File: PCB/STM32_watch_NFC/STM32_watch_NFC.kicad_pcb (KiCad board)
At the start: 4 copper layers, 70 x 100 mm, 287 parts, among them J1 Conn_01x06_Socket, J2 USB_C_Receptacle_PowerOnly_6P, Q1 2N7000, SW1 SW_DPST_x2, SW2 SW_DPST_x2, SW3 SW_DPST_x2, U1 STM32L031G6Ux, U2 MIC5365-3.3YC5, U3 ST25R3916-AQWT, U4 MT3608, Y1 27.12Mhz, Y2 32.768kHz

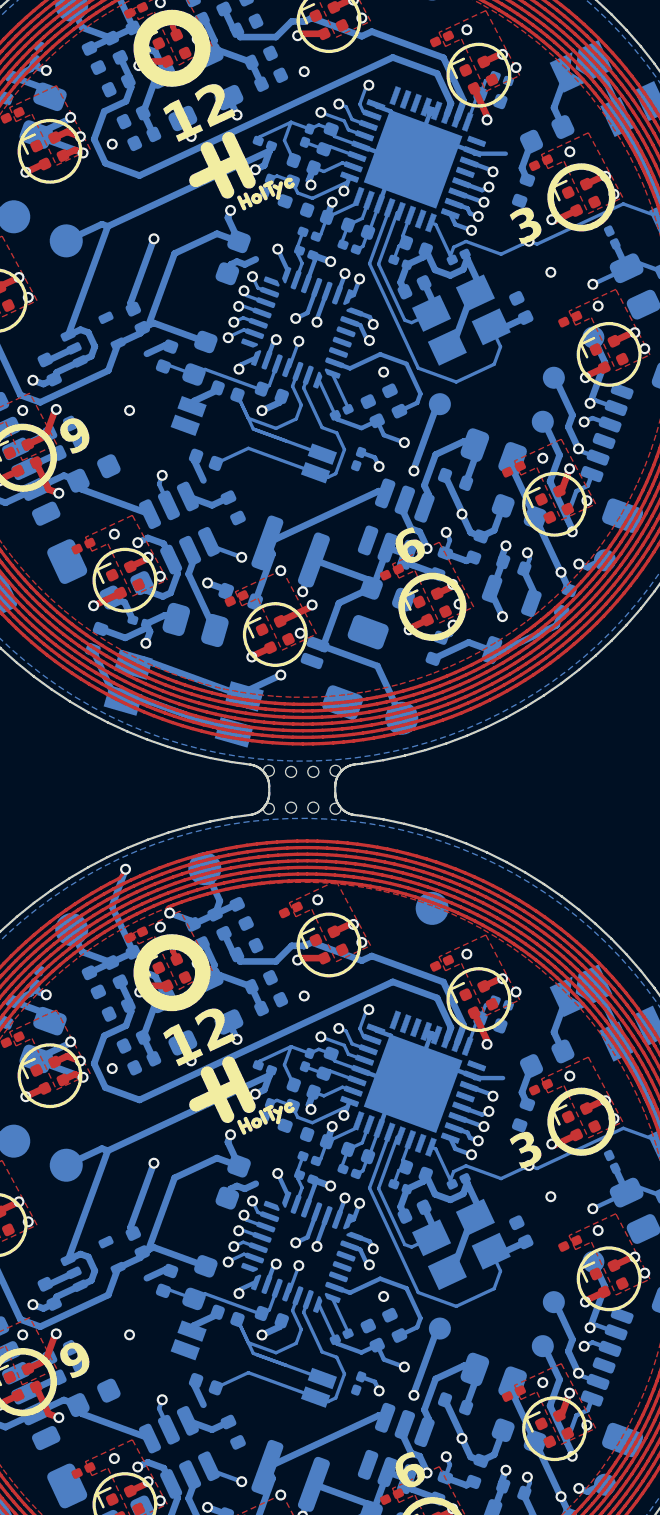
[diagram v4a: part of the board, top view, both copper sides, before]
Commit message: CODING #5 working Time and ADC for battery value
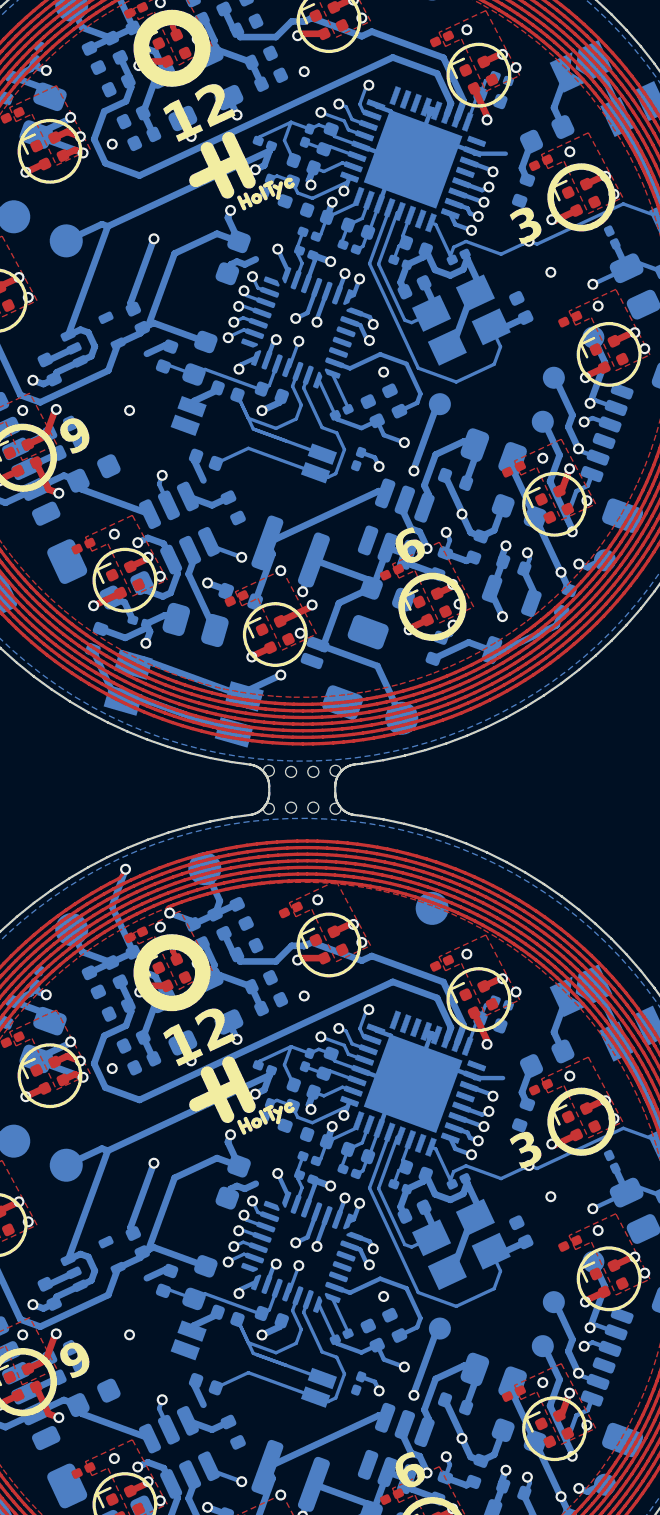
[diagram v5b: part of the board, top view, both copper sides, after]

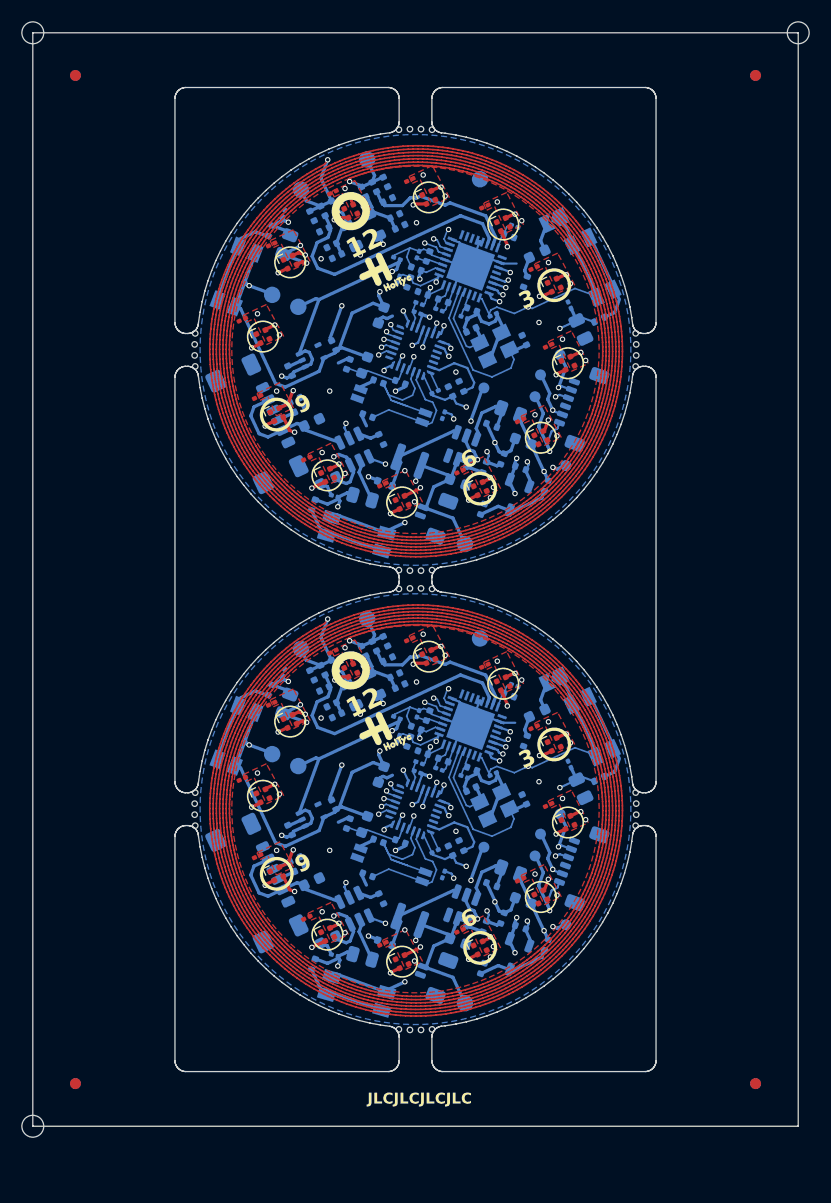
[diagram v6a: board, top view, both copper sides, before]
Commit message: URX watch #1
pcb is NOT panelizated
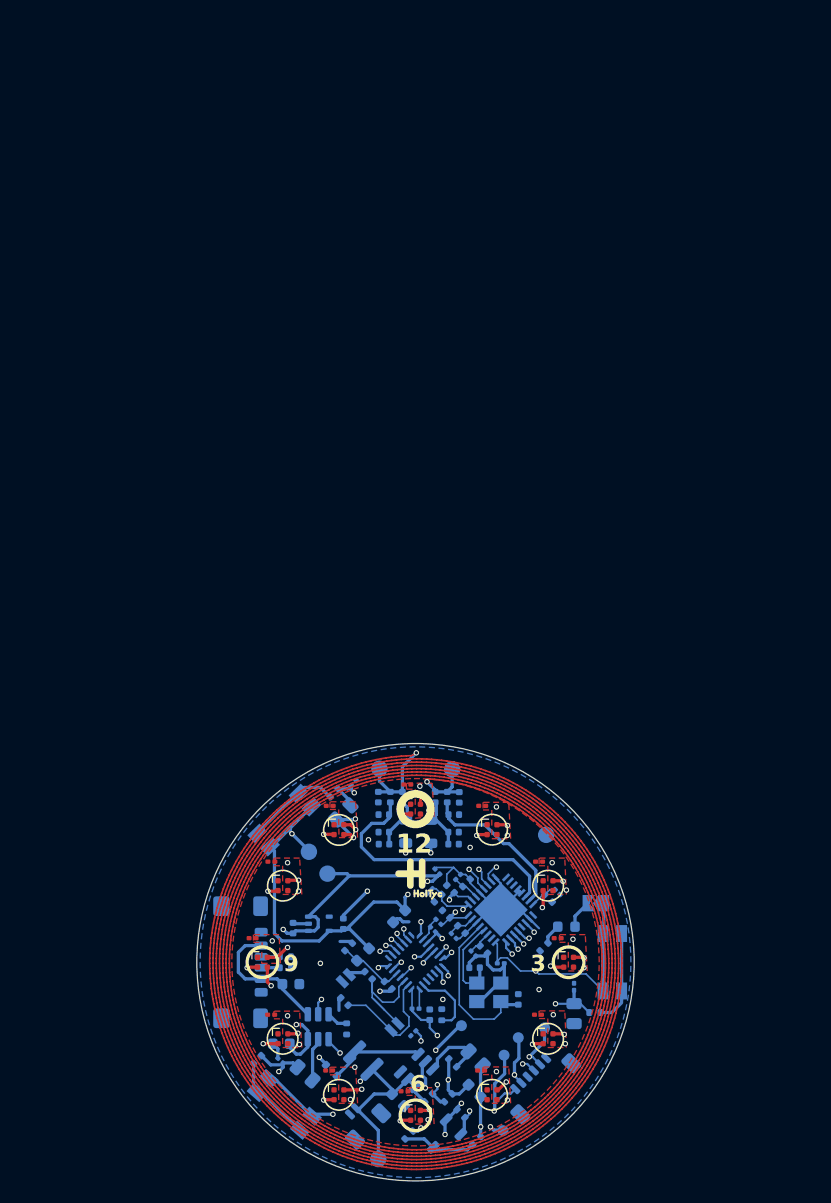
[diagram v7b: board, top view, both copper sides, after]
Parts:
- removed the +BAT at (153.0, 108.8)
- removed the +BAT at (153.0, 66.8)
- removed the 3V3 at (135.4, 44.0)
- removed the 3V3 at (135.4, 86.0)
- removed the 5V at (137.8, 87.1)
- removed the 5V at (137.8, 45.1)
- removed the A1 at (138.0, 34.4)
- removed the A1 at (138.0, 76.4)
- removed the A2 at (144.1, 31.6)
- removed the A2 at (144.1, 73.6)
- removed the CLK at (159.4, 53.3)
- removed the CLK at (159.4, 95.3)
- removed the DINS at (162.3, 59.6)
- removed the DINS at (162.3, 101.6)
- removed the DIO at (159.9, 93.3)
- removed the DIO at (159.9, 51.3)
- removed the D_BAT at (154.8, 52.5)
- removed the D_BAT at (154.8, 94.5)
- removed the G*** at (145.8, 41.9)
- removed the G*** at (145.8, 83.9)
- removed the GND at (154.4, 33.4)
- removed the GND at (154.4, 75.4)
- removed the JP1 at (161.2, 37.1)
- removed the JP1 at (161.2, 79.1)
- removed KiKit_FID_B_1, KiKit_FID_B_2, KiKit_FID_B_3, KiKit_FID_B_4, KiKit_FID_T_1, KiKit_FID_T_2, KiKit_FID_T_3, KiKit_FID_T_4: Fiducial, Fiducial
- removed KiKit_MB_1_1, KiKit_MB_1_2, KiKit_MB_1_3, KiKit_MB_1_4, KiKit_MB_2_1, KiKit_MB_2_2, KiKit_MB_2_3, KiKit_MB_2_4, KiKit_MB_3_1, KiKit_MB_3_2, KiKit_MB_3_3, KiKit_MB_3_4, KiKit_MB_4_1, KiKit_MB_4_2, KiKit_MB_4_3, KiKit_MB_4_4, KiKit_MB_5_1, KiKit_MB_5_2, KiKit_MB_5_3, KiKit_MB_5_4, KiKit_MB_6_1, KiKit_MB_6_2, KiKit_MB_6_3, KiKit_MB_6_4, KiKit_MB_7_1, KiKit_MB_7_2, KiKit_MB_7_3, KiKit_MB_7_4, KiKit_MB_8_1, KiKit_MB_8_2, KiKit_MB_8_3, KiKit_MB_8_4, KiKit_TO_1, KiKit_TO_2, KiKit_TO_3: NPTH, NPTH
- removed the NRST at (161.7, 91.5)
- removed the NRST at (161.7, 49.5)
- removed TC1, TC12, TC13, TC14, TC15, TC16, TC17, TC18, TC19, TC2, TC20, TC21, TC22, TC23, TC28, TC29, TC30, TC31, TC7: 100n, Capacitor_SMD:C_0201_0603Metric
- removed TC10, TC11, TC46, TC5, TC6: 1u, Capacitor_SMD:C_0402_1005Metric
- removed TC24, TC25, TC26, TC27, TC4: 10u, Capacitor_SMD:C_0603_1608Metric
- removed TC3: 10n, Capacitor_SMD:C_0402_1005Metric
- removed TC34, TC36, TC38, TC40, TC42, TC44, TC47: 22n, Capacitor_SMD:C_0201_0603Metric
- removed TC35, TC37, TC39, TC41, TC43, TC45: 2.2uF, Capacitor_SMD:C_0402_1005Metric
- removed TC48, TC49, TC50, TC51, TC58, TC59, TC8, TC9: 15pF, Capacitor_SMD:C_0402_1005Metric
- removed TC52, TC53, TC54, TC55, TC57, TC61: 220pF, Capacitor_SMD:C_0402_1005Metric
- removed TC56, TC60: 10pF, Capacitor_SMD:C_0402_1005Metric
- removed TD1, TD10, TD11, TD12, TD2, TD3, TD4, TD5, TD6, TD7, TD8, TD9: SK6805, LED_SMD:LED_SK6812_EC15_1.5x1.5mm
- removed TD13: D_Schottky, Diode_SMD:D_SOD-523
- removed TD14: LED, LED_SMD:LED_0603_1608Metric
- removed TFB1: FerriteBead, Inductor_SMD:L_0603_1608Metric
- removed TJ1: Conn_01x06_Socket, Connector_JST:JST_SUR_SM06B-SURS-TF_1x06-1MP_P0.80mm_Horizontal
- removed TJ2: USB_C_Receptacle_PowerOnly_6P, Connector_USB:USB_C_Receptacle_GCT_USB4135-GF-A_6P_TopMnt_Horizontal
- removed TL1: 22uH, Components:SLW3015
- removed TL2, TL3: 270nH 500mOhm, Inductor_SMD:L_0805_2012Metric
- removed TLi-po1: Conn_01x02_Socket, Connector_JST:JST_SUR_SM02B-SURS-TF_1x02-1MP_P0.80mm_Horizontal
- removed TME4055A1: ~, Package_TO_SOT_SMD:SOT-23-6
- removed TQ1: 2N7000, Package_TO_SOT_SMD:TSOT-23
- removed TR1, TR16, TR17, TR2, TR3: 10K, Resistor_SMD:R_0402_1005Metric
- removed TR10, TR12, TR14, TR8: 16.5K, Resistor_SMD:R_0805_2012Metric
- removed TR11, TR13, TR15, TR18, TR6: 510, Resistor_SMD:R_0402_1005Metric
- removed TR4, TR5, TR7: 5K1, Resistor_SMD:R_0402_1005Metric
- removed TR9: 2.2K, Resistor_SMD:R_0402_1005Metric
- removed TSW1, TSW2, TSW3: SW_DPST_x2, Button_Switch_SMD:Panasonic_EVQPUJ_EVQPUA
- removed TU1: STM32L031G6Ux, Package_DFN_QFN:QFN-28_4x4mm_P0.5mm
- removed TU2: MIC5365-3.3YC5, Package_TO_SOT_SMD:SOT-353_SC-70-5
- removed TU3: ST25R3916-AQWT, ST25R3916-AQWT:QFN50P500X500X100-33N
- removed TU4: MT3608, Package_TO_SOT_SMD:SOT-23-6
- removed TY1: 27.12Mhz, Crystal:Crystal_SMD_3225-4Pin_3.2x2.5mm
- removed TY2: 32.768kHz, Crystal:Crystal_SMD_SeikoEpson_MC146-4Pin_6.7x1.5mm
- added +BAT: 2.7-4.2V, TestPoint:TestPoint_Pad_D1.5mm, B.Cu at (145.1, 123.0)
- added 3V3: 3V3, TestPoint:TestPoint_Pad_D1.5mm, B.Cu at (138.8, 94.9)
- added 5V: 5V, TestPoint:TestPoint_Pad_D1.5mm, B.Cu at (140.4, 96.9)
- added A1: ~, TestPoint:TestPoint_Pad_D1.5mm, B.Cu at (145.2, 87.3)
- added A2: ~, TestPoint:TestPoint_Pad_D1.5mm, B.Cu at (151.8, 87.3)
- added CLK: ~, TestPoint:TestPoint_Pad_D1.0mm, B.Cu at (156.6, 113.5)
- added DINS: ~, TestPoint:TestPoint_Pad_D1.0mm, B.Cu at (156.5, 120.4)
- added DIO: ~, TestPoint:TestPoint_Pad_D1.0mm, B.Cu at (157.9, 111.9)
- added D_BAT: ~, TestPoint:TestPoint_Pad_D1.0mm, B.Cu at (152.7, 110.8)
- added G***: LOGO, LOGO, F.Cu at (149.1, 97.5)
- added GND: GND, TestPoint:TestPoint_Pad_D1.5mm, B.Cu at (160.4, 93.3)
- added JP1: SolderJumper_2_Open, Jumper:SolderJumper-2_P1.3mm_Open_TrianglePad1.0x1.5mm, B.Cu at (165.0, 99.6)
- added NRST: ~, TestPoint:TestPoint_Pad_D1.0mm, B.Cu at (160.3, 111.0)
- moved SW2 21.6 mm to (166.5, 105.0), turned to 90 degrees
- moved R15 21.4 mm to (164.9, 109.6), turned to 180 degrees
- moved R14 20.6 mm to (163.0, 109.7), turned to -90 degrees
- moved C30 20.3 mm to (163.0, 107.2), turned to -90 degrees
- moved J1 20.1 mm to (159.8, 116.0), turned to -135 degrees
- moved D4 20.0 mm to (162.5, 105.0), turned to 0 degrees
- moved D5 19.9 mm to (160.6, 112.0), turned to 0 degrees
- moved D14 19.7 mm to (162.3, 101.8), turned to 0 degrees
- moved C15 19.4 mm to (161.5, 102.8), turned to 0 degrees
- moved C47 19.3 mm to (161.5, 98.6), turned to -45 degrees
- moved C16 19.2 mm to (159.7, 109.8), turned to 0 degrees
- moved R2 19.0 mm to (154.1, 121.3), turned to -135 degrees
- moved C46 18.9 mm to (160.7, 99.2), turned to 135 degrees
- moved D3 18.9 mm to (160.6, 98.0), turned to 0 degrees
- moved R18 18.9 mm to (160.2, 103.6), turned to -135 degrees
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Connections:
- net Board_1-+3.3V renamed +3.3V
- net Board_1-+3.3VA renamed +3.3VA
- net Board_1-+5V renamed +5V
- net Board_1-+BATT renamed +BATT
- net Board_1-/LSE_IN renamed /LSE_IN
- net Board_1-/LSE_OUT renamed /LSE_OUT
- net Board_1-/NFC_RFID/A1 renamed /NFC_RFID/A1
- net Board_1-/NFC_RFID/A2 renamed /NFC_RFID/A2
- net Board_1-/NRST renamed /NRST
- net Board_1-/SWCLK renamed /SWCLK
- net Board_1-/SWDIO renamed /SWDIO
- net Board_1-BATT_STM renamed BATT_STM
- net Board_1-Button_LB renamed Button_LB
- net Board_1-Button_LT renamed Button_LT
- net Board_1-Button_R renamed Button_R
- net Board_1-CHRG_STM renamed CHRG_STM
- net Board_1-DIN_LED renamed DIN_LED
- net Board_1-DIN_STM renamed DIN_STM
- net Board_1-DONE_STM renamed DONE_STM
- net Board_1-GND renamed GND
- net Board_1-Net-(C50-Pad1) renamed Net-(C50-Pad1)
- net Board_1-Net-(C51-Pad1) renamed Net-(C51-Pad1)
- net Board_1-Net-(D1-DIN) renamed Net-(D1-DIN)
- net Board_1-Net-(D1-DOUT) renamed Net-(D1-DOUT)
- net Board_1-Net-(D10-DIN) renamed Net-(D10-DIN)
- net Board_1-Net-(D10-DOUT) renamed Net-(D10-DOUT)
- net Board_1-Net-(D11-DOUT) renamed Net-(D11-DOUT)
- net Board_1-Net-(D13-A) renamed Net-(D13-A)
- net Board_1-Net-(D14-K) renamed Net-(D14-K)
- net Board_1-Net-(D2-DOUT) renamed Net-(D2-DOUT)
- net Board_1-Net-(D3-DOUT) renamed Net-(D3-DOUT)
- net Board_1-Net-(D4-DOUT) renamed Net-(D4-DOUT)
- net Board_1-Net-(D5-DOUT) renamed Net-(D5-DOUT)
- net Board_1-Net-(D7-DIN) renamed Net-(D7-DIN)
- net Board_1-Net-(D7-DOUT) renamed Net-(D7-DOUT)
- net Board_1-Net-(D8-DOUT) renamed Net-(D8-DOUT)
- net Board_1-Net-(J2-CC1) renamed Net-(J2-CC1)
- net Board_1-Net-(J2-CC2) renamed Net-(J2-CC2)
- net Board_1-Net-(ME4055A1-PROG) renamed Net-(ME4055A1-PROG)
- net Board_1-Net-(SW1A-A) renamed Net-(SW1A-A)
- net Board_1-Net-(SW2A-A) renamed Net-(SW2A-A)
- net Board_1-Net-(SW3A-A) renamed Net-(SW3A-A)
- net Board_1-Net-(U1-BOOT0) renamed Net-(U1-BOOT0)
- net Board_1-Net-(U3-AGDC) renamed Net-(U3-AGDC)
- net Board_1-Net-(U3-RFI1) renamed Net-(U3-RFI1)
- net Board_1-Net-(U3-RFI2) renamed Net-(U3-RFI2)
- net Board_1-Net-(U3-RFO1) renamed Net-(U3-RFO1)
- net Board_1-Net-(U3-RFO2) renamed Net-(U3-RFO2)
- net Board_1-Net-(U3-VDD_A) renamed Net-(U3-VDD_A)
- net Board_1-Net-(U3-VDD_AM) renamed Net-(U3-VDD_AM)
- net Board_1-Net-(U3-VDD_D) renamed Net-(U3-VDD_D)
- net Board_1-Net-(U3-VDD_DR) renamed Net-(U3-VDD_DR)
- net Board_1-Net-(U3-XTI) renamed Net-(U3-XTI)
- net Board_1-Net-(U3-XTO) renamed Net-(U3-XTO)
- net Board_1-Net-(U4-FB) renamed Net-(U4-FB)
- net Board_1-SPI_CS_STM renamed SPI_CS_STM
- net Board_1-SPI_IRQ_STM renamed SPI_IRQ_STM
- net Board_1-SPI_MISO_STM renamed SPI_MISO_STM
- net Board_1-SPI_MOSI_STM renamed SPI_MOSI_STM
- net Board_1-SPI_SCL_STM renamed SPI_SCL_STM
- net Board_1-VBUS renamed VBUS
- D14 pad 2: Board_1-Net-(D14-A) -> Net-(D14-A)
- D6 pad 1: Board_1-unconnected-(D6-DOUT-Pad1) -> unconnected-(D6-DOUT-Pad1)
- J1 pad 1: Board_1-unconnected-(J1-Pin_1-Pad1) -> unconnected-(J1-Pin_1-Pad1)
- U1 pad 14: Board_1-unconnected-(U1-PB0-Pad14) -> unconnected-(U1-PB0-Pad14)
- U1 pad 24: Board_1-unconnected-(U1-PB3-Pad24) -> unconnected-(U1-PB3-Pad24)
- U1 pad 25: Board_1-unconnected-(U1-PB6-Pad25) -> unconnected-(U1-PB6-Pad25)
- U1 pad 26: Board_1-unconnected-(U1-PB7-Pad26) -> unconnected-(U1-PB7-Pad26)
- U1 pad 8: Board_1-unconnected-(U1-PA2-Pad8) -> unconnected-(U1-PA2-Pad8)
- U2 pad 4: Board_1-unconnected-(U2-NC-Pad4) -> unconnected-(U2-NC-Pad4)
- U3 pad 17: Board_1-unconnected-(U3-EXT_LM-Pad17) -> unconnected-(U3-EXT_LM-Pad17)
- U3 pad 18: Board_1-unconnected-(U3-AAT_A-Pad18) -> unconnected-(U3-AAT_A-Pad18)
- U3 pad 19: Board_1-unconnected-(U3-AAT_B-Pad19) -> unconnected-(U3-AAT_B-Pad19)
- U3 pad 2: Board_1-unconnected-(U3-CSO-Pad2) -> unconnected-(U3-CSO-Pad2)
- U3 pad 25: Board_1-unconnected-(U3-CSI-Pad25) -> unconnected-(U3-CSI-Pad25)
- U3 pad 28: Board_1-unconnected-(U3-MCU_CLK-Pad28) -> unconnected-(U3-MCU_CLK-Pad28)
- U4 pad 6: Board_1-unconnected-(U4-NC-Pad6) -> unconnected-(U4-NC-Pad6)
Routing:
- net Board_0-/NFC_RFID/A1: track 797.8 -> 0.00 mm, vias 1 -> 0
- net Board_0-GND: track 237.5 -> 0.00 mm, vias 32 -> 0
- net Board_0-+3.3V: track 152.2 -> 0.00 mm, vias 8 -> 0
- net Board_0-+5V: track 76.9 -> 0.00 mm, vias 6 -> 0
- net Board_0-/NRST: track 33.8 -> 0.00 mm, vias 3 -> 0
- net Board_0-+BATT: track 32.1 -> 0.00 mm, vias 2 -> 0
- net Board_0-/SWCLK: track 24.5 -> 0.00 mm, vias 2 -> 0
- net Board_0-Net-(U3-RFI1): track 24.3 -> 0.00 mm
- net Board_0-Button_LT: track 24.3 -> 0.00 mm, vias 2 -> 0
- net Board_0-DIN_STM: track 23.0 -> 0.00 mm, vias 4 -> 0
- net Board_0-BATT_STM: track 22.4 -> 0.00 mm, vias 3 -> 0
- net Board_0-Button_LB: track 21.9 -> 0.00 mm, vias 2 -> 0
- net Board_0-/SWDIO: track 21.5 -> 0.00 mm, vias 2 -> 0
- net Board_0-SPI_IRQ_STM: track 20.2 -> 0.00 mm, vias 2 -> 0
- net Board_0-SPI_CS_STM: track 19.5 -> 0.00 mm, vias 2 -> 0
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- removed copper zone on F.Cu, net Board_0-+5V
- removed copper zone on B.Cu, net Board_0-GND
- removed copper zone on F.Cu, net Board_0-GND
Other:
- board size 70 x 100 mm -> 40 x 40 mm
